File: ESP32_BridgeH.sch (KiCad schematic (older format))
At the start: 24 parts, among them J1 MT1, J2 MT2, J3 boot, J4 Serial, SW1 reset, U1 TB6612FNG, U2 ESP32-WROOM, U3 MPU6050, U4 LM7805_TO220

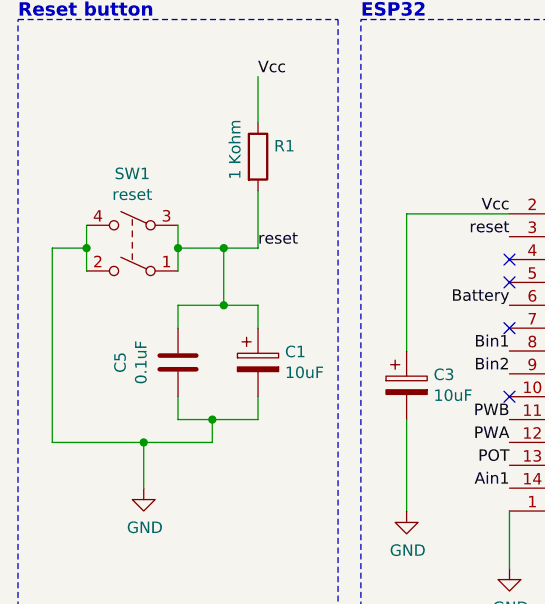
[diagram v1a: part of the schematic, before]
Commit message: fix button problem
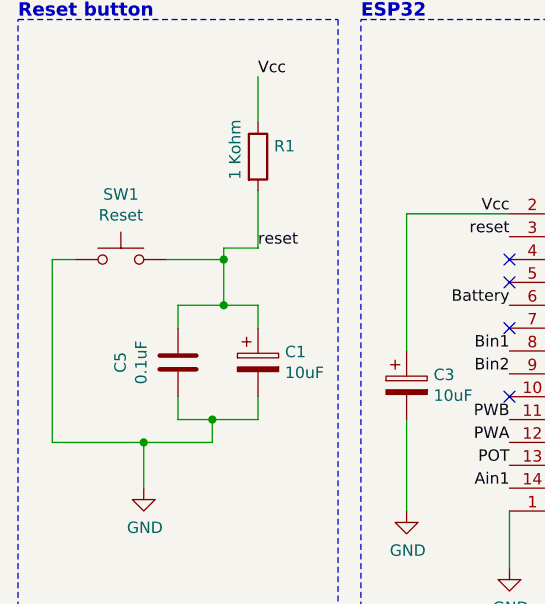
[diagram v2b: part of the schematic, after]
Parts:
- removed SW1: reset, digikey-footprints:Switch_Tactile_THT_6x6mm, symbol Switch:SW_DPST
- added SW1: Reset, Button_Switch_THT:SW_PUSH_6mm, symbol Switch:SW_Push
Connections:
- net GND: now also SW1.1
- net reset: now also SW1.2
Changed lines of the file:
@@
 EESchema Schematic File Version 4
-LIBS:ESP32_BridgeH-cache
-EELAYER 29 0
+EELAYER 30 0
 EELAYER END
 $Descr A4 11693 8268
@@
 Wire Notes Line
 	2350 5450 2350 2500
-$Comp
-L Switch:SW_DPST SW1
-U 1 1 5EDE5818
-P 2850 3500
-F 0 "SW1" H 2850 3825 50  0000 C CNN
-F 1 "reset" H 2850 3734 50  0000 C CNN
-F 2 "digikey-footprints:Switch_Tactile_THT_6x6mm" H 2850 3500 50  0001 C CNN
-F 3 "~" H 2850 3500 50  0001 C CNN
-	1    2850 3500
-	-1   0    0    -1
-$EndComp
 Text Label 3400 3500 0    50   ~ 0
 reset
@@
 Boot
 Wire Wire Line
-	3050 3400 3050 3500
-Wire Wire Line
 	3400 3250 3400 3500
 Wire Wire Line
-	2650 3400 2650 3500
-Wire Wire Line
-	2650 3500 2500 3500
-Wire Wire Line
-	2500 3500 2500 4350
-Connection ~ 2650 3500
-Wire Wire Line
-	2650 3500 2650 3600
-Connection ~ 3050 3500
-Wire Wire Line
-	3050 3500 3050 3600
-Wire Wire Line
 	2900 4350 3200 4350
 Wire Wire Line
@@
 	3400 3750 3400 3850
 Wire Wire Line
-	3250 3750 3250 3500
-Wire Wire Line
-	3050 3500 3250 3500
+	3250 3750 3250 3550
 Connection ~ 3250 3750
 Wire Wire Line
 	3250 3750 3400 3750
-Connection ~ 3250 3500
 Wire Wire Line
 	3250 3500 3400 3500
@@
 Text Label 7350 1900 2    50   ~ 0
 POT
+$Comp
+L Switch:SW_Push SW1
+U 1 1 5F0B3F20
+P 2800 3550
+F 0 "SW1" H 2800 3835 50  0000 C CNN
+F 1 "Reset" H 2800 3744 50  0000 C CNN
+F 2 "Button_Switch_THT:SW_PUSH_6mm" H 2800 3750 50  0001 C CNN
+F 3 "~" H 2800 3750 50  0001 C CNN
+	1    2800 3550
+	1    0    0    -1
+$EndComp
+Wire Wire Line
+	3000 3550 3250 3550
+Connection ~ 3250 3550
+Wire Wire Line
+	3250 3550 3250 3500
+Wire Wire Line
+	2600 3550 2500 3550
+Wire Wire Line
+	2500 3550 2500 4350
 $EndSCHEMATC
